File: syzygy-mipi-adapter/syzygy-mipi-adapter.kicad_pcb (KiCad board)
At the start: 4 copper layers, 45 x 70 mm, 98 parts, among them J1 Conn_02x06_Odd_Even, J2 SYZYGY_STD, J3 USB_C_Receptacle_USB2.0_16P, J4 SM03B-SRSS-TB, J6 501951-2230, J7 501951-2230, J8 501951-2230, Q1 DMG1024UV-7, Q2 DMG1024UV-7, U1 RP2350_80QFN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

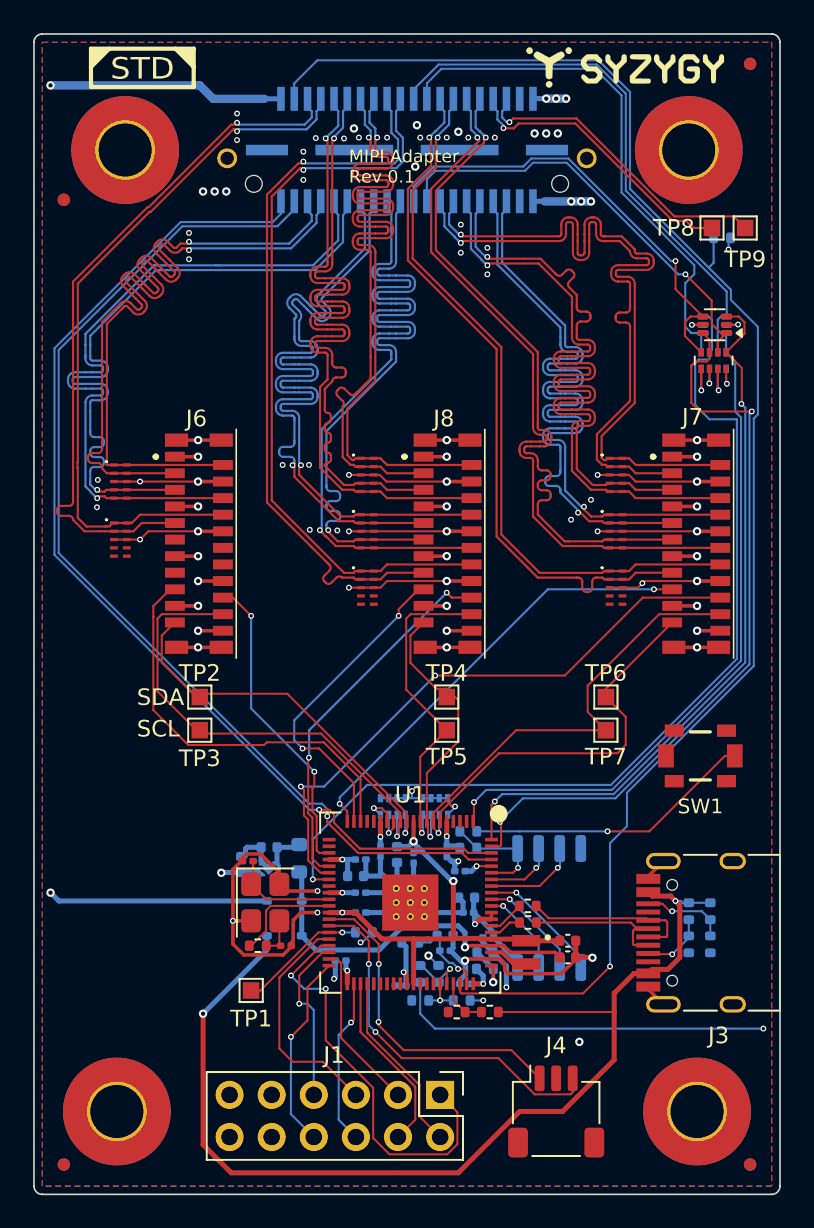
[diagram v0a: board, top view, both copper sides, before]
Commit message: Update stack-up. Adjust DP trace width and spacing to 100 ohm impedance.
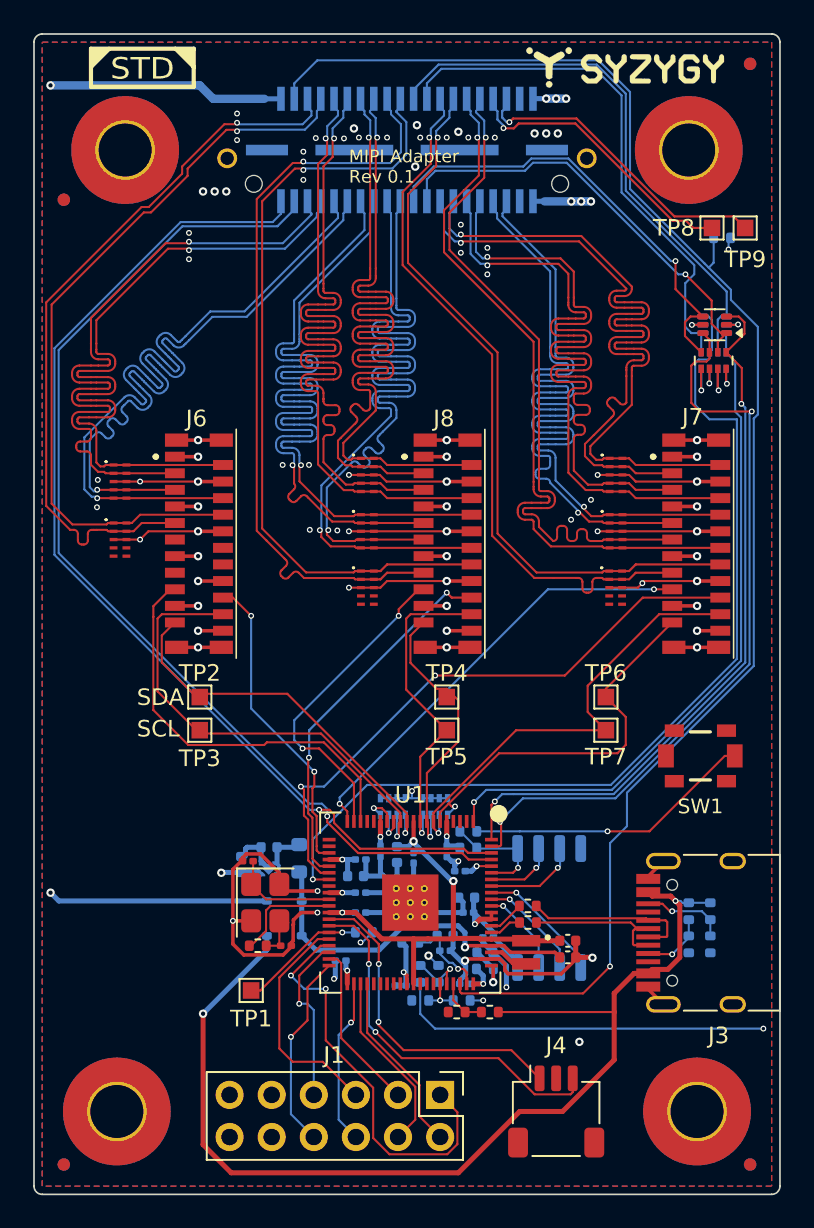
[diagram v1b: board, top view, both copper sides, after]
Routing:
- net /D0N: track 43.2 -> 45.2 mm
- net /D0P: track 42.1 -> 44.1 mm
- net /D3N: track 44.0 -> 46.0 mm
- net /D7P: track 44.3 -> 46.3 mm
- net /D7N: track 45.3 -> 47.3 mm
- net /D4N: track 45.1 -> 47.1 mm
- net /D4P: track 44.1 -> 46.1 mm
- net /D1N: track 43.4 -> 45.3 mm
- net /D1P: track 42.3 -> 44.3 mm
- net /D2P: track 43.2 -> 45.2 mm
- net /D2N: track 42.1 -> 44.1 mm
- net /D6N: track 44.1 -> 46.0 mm
- net /D6P: track 45.2 -> 47.1 mm
- net /D3P: track 45.2 -> 47.1 mm
- net /D5P: track 44.1 -> 46.1 mm
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
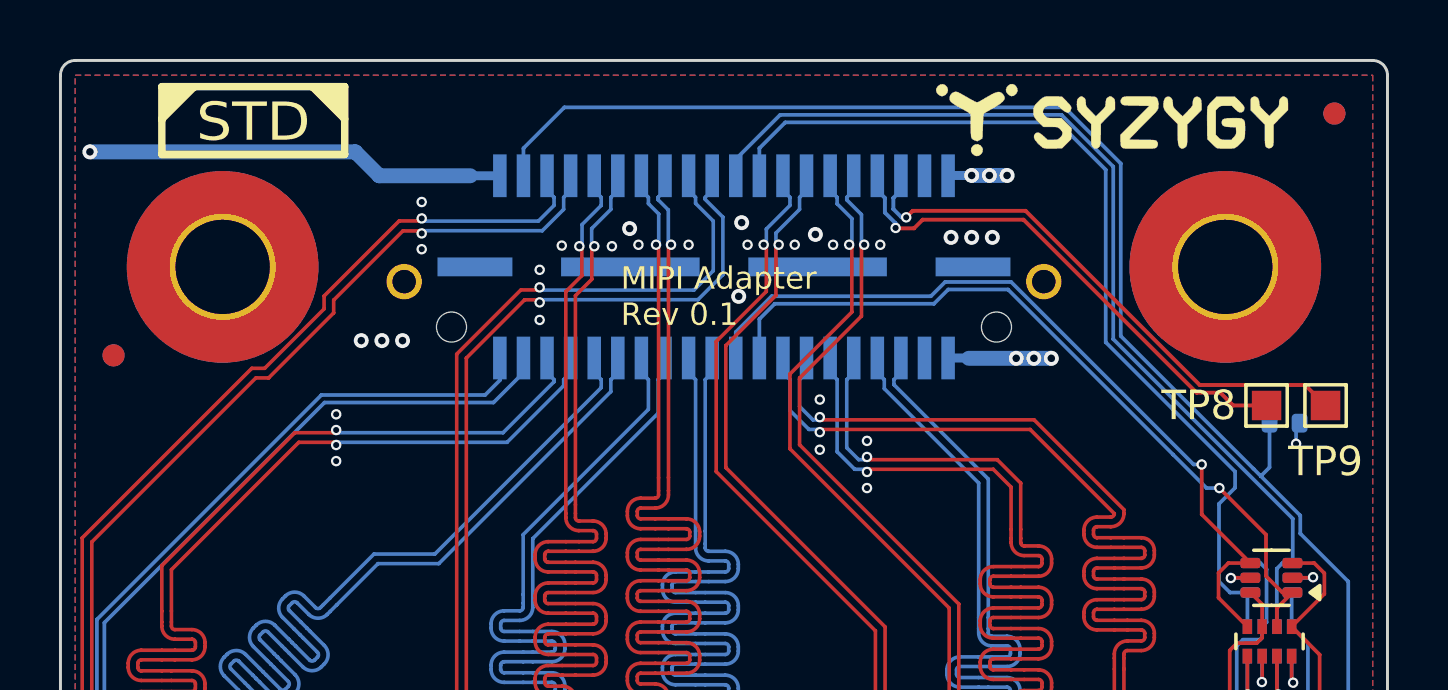
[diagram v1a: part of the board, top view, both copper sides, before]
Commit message: Made tinyvision logo bigger
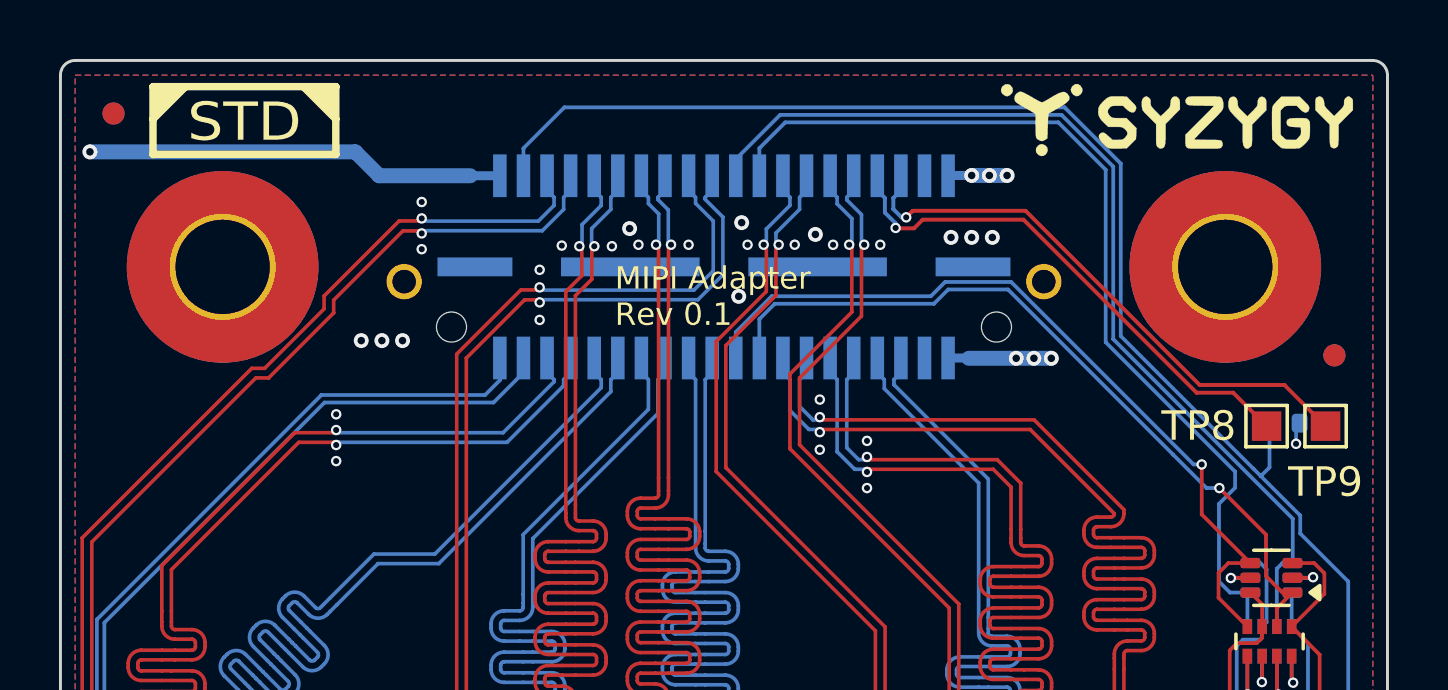
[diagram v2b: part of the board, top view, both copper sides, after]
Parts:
- C38: value 2.2u -> 10u
- LOGO4: footprint CUSTOM:tinyAI_logo -> CUSTOM:tinyAI_4_5mm
- moved FID1 8.20 mm to (101.8, 61.8)
- moved FID2 8.20 mm to (143.2, 70.0)
- moved FID5 8.20 mm to (101.8, 61.8)
- moved FID6 8.20 mm to (143.2, 70.0)
- moved LOGO2 2.20 mm to (137.8, 62.0)
- moved TP8 0.70 mm to (140.9, 72.4)
- moved TP9 0.70 mm to (142.9, 72.4)
- moved LOGO1 0.30 mm to (109.3, 63.2)

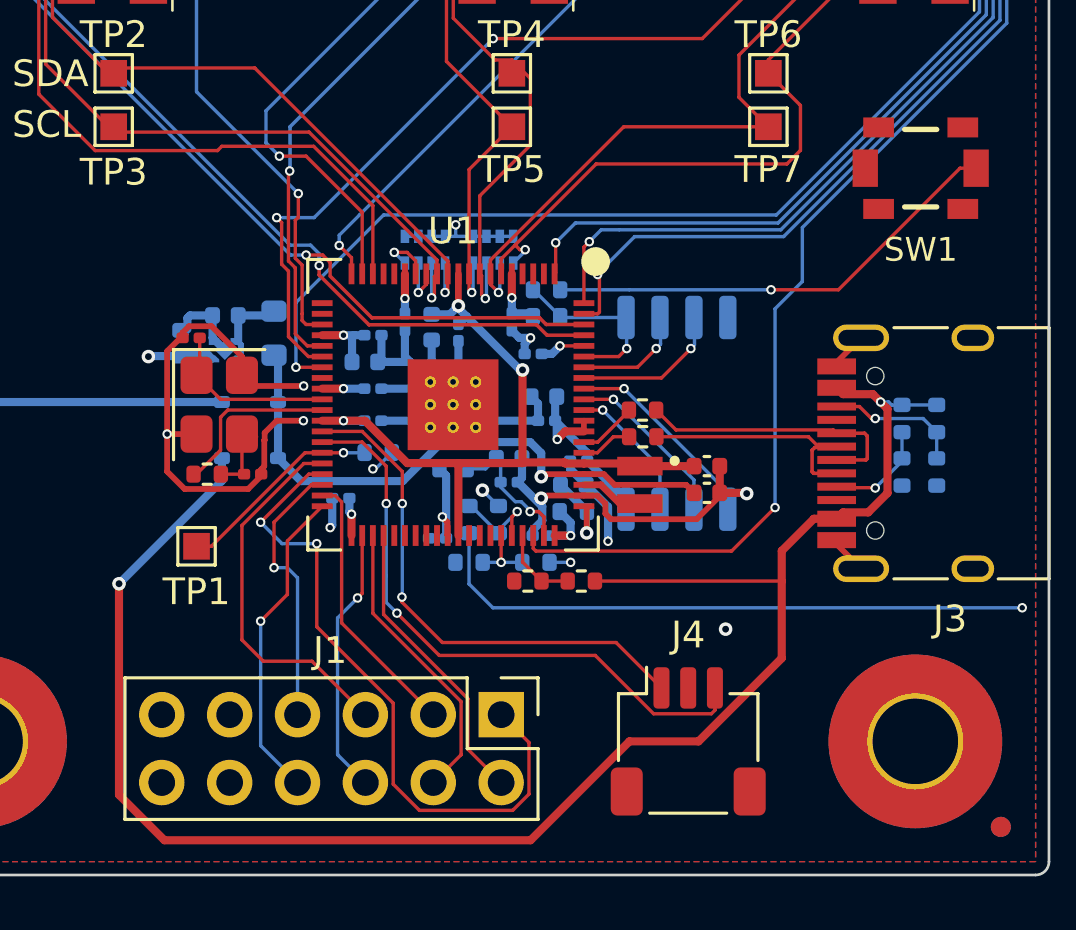
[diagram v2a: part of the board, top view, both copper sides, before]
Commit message: Add a few more vias
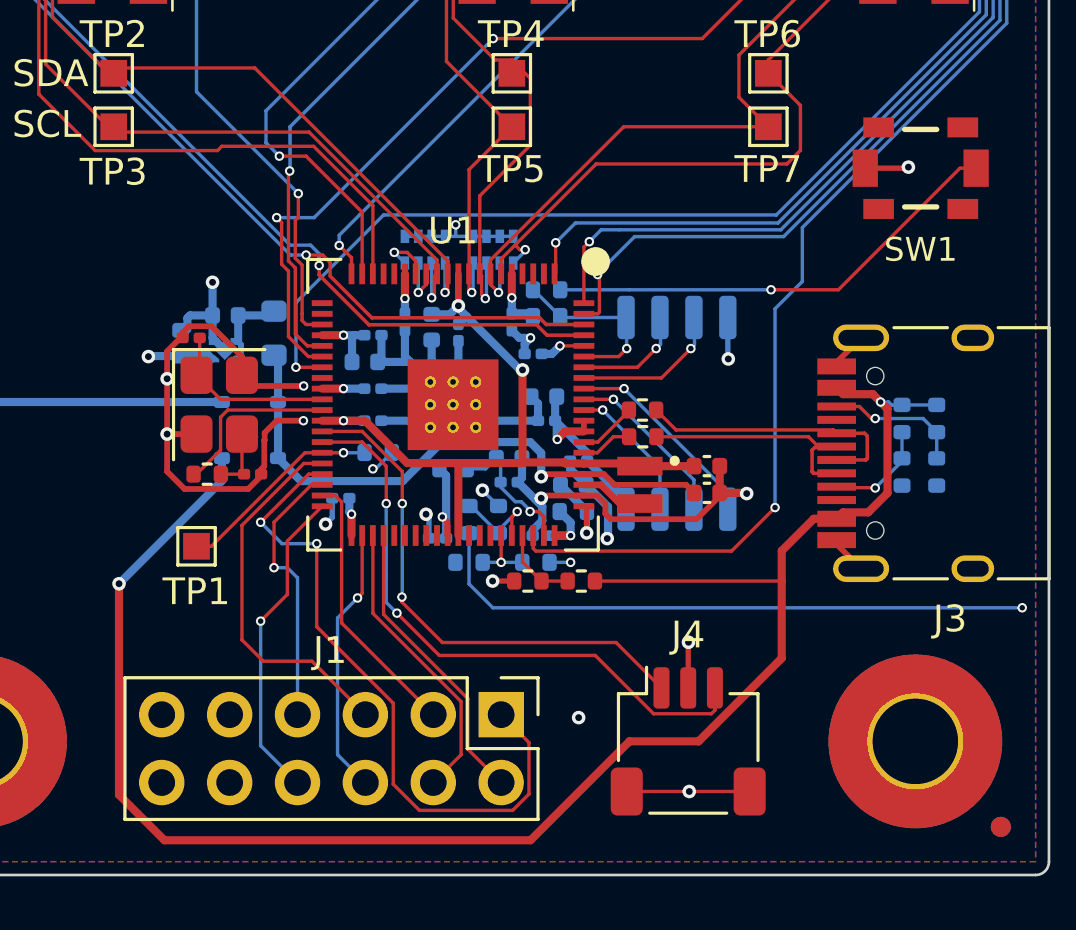
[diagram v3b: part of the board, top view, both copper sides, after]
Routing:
- net GND: track 156.0 -> 168.4 mm, vias 81 -> 89
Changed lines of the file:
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@@
 			(keep_text_aligned yes)
 		)
-		(gr_text "5.0 mm"
+		(gr_text "196.9 mils"
 			(at 95.1 126.3 90)
 			(layer "Dwgs.User")
@@
 			(keep_text_aligned yes)
 		)
-		(gr_text "6.0 mm"
+		(gr_text "236.2 mils"
 			(at 90.6 126.5 90)
 			(layer "Dwgs.User")
@@
 			(keep_text_aligned yes)
 		)
-		(gr_text "24.5 mm"
+		(gr_text "964.6 mils"
 			(at 112.25 137.95 0)
 			(layer "Dwgs.User")
@@
 			(keep_text_aligned yes)
 		)
-		(gr_text "13.260 mm"
+		(gr_text "522.060 mils"
 			(at 106.63016 50.35 0)
 			(layer "Dwgs.User")
@@
 			(keep_text_aligned yes)
 		)
-		(gr_text "9.04 mm"
+		(gr_text "355.91 mils"
 			(at 90.6 64.5 90)
 			(layer "Dwgs.User")
@@
 			(keep_text_aligned yes)
 		)
-		(gr_text "5.0 mm"
+		(gr_text "196.9 mils"
 			(at 103.4 134.3 0)
 			(layer "Dwgs.User")
@@
 			(keep_text_aligned yes)
 		)
-		(gr_text "12.0000 mm"
+		(gr_text "472.4406 mils"
 			(at 148.55 66.000005 90)
 			(layer "Dwgs.User")
@@
 	)
 	(segment
+		(start 138.125 103.55)
+		(end 139.7 103.55)
+		(width 0.2)
+		(layer "F.Cu")
+		(net 2)
+	)
+	(segment
 		(start 115.63595 114.70405)
 		(end 115.52 114.82)
@@
 	(segment
 		(start 112 110.4)
-		(end 112 113.5)
+		(end 112 111.43)
 		(width 0.2159)
 		(layer "F.Cu")
@@
 	)
 	(segment
+		(start 131.5 121.3)
+		(end 131.51 121.29)
+		(width 0.2)
+		(layer "F.Cu")
+		(net 2)
+	)
+	(segment
 		(start 104.824 90.5)
 		(end 105.6 90.5)
@@
 	)
 	(segment
+		(start 131.54 126.875)
+		(end 133.8 126.875)
+		(width 0.127)
+		(layer "F.Cu")
+		(net 2)
+	)
+	(segment
 		(start 115.031926 115.55595)
 		(end 112.65595 115.55595)
@@
 	)
 	(segment
+		(start 131.5 123)
+		(end 131.5 121.3)
+		(width 0.2)
+		(layer "F.Cu")
+		(net 2)
+	)
+	(segment
 		(start 135.5 86.6)
 		(end 135.9 86.6)
@@
 	)
 	(segment
+		(start 112 111.43)
+		(end 112 113.5)
+		(width 0.2159)
+		(layer "F.Cu")
+		(net 2)
+	)
+	(segment
 		(start 137.055 110.813475)
 		(end 137.97 109.898475)
@@
 	)
 	(segment
+		(start 139.7 103.55)
+		(end 139.74 103.51)
+		(width 0.2)
+		(layer "F.Cu")
+		(net 2)
+	)
+	(segment
 		(start 141.3 97)
 		(end 140 97)
@@
 	)
 	(segment
+		(start 129.2 126.875)
+		(end 131.54 126.875)
+		(width 0.127)
+		(layer "F.Cu")
+		(net 2)
+	)
+	(segment
 		(start 132.68 115.82)
 		(end 132.68 115.7)
@@
 	)
 	(segment
+		(start 124.99 119)
+		(end 124.18 119)
+		(width 0.2)
+		(layer "F.Cu")
+		(net 2)
+	)
+	(segment
 		(start 119.724 86.6)
 		(end 120.5 86.6)
@@
 	)
 	(via
-		(at 128.5 117.5097)
-		(size 0.3556)
-		(drill 0.2032)
+		(at 128.47 117.41)
+		(size 0.508)
+		(drill 0.254)
 		(layers "F.Cu" "B.Cu")
 		(net 2)
@@
 	)
 	(via
+		(at 133 110.69)
+		(size 0.508)
+		(drill 0.254)
+		(layers "F.Cu" "B.Cu")
+		(net 2)
+	)
+	(via
 		(at 119 90)
 		(size 0.3556)
@@
 	)
 	(via
+		(at 127.4 124.11)
+		(size 0.508)
+		(drill 0.254)
+		(layers "F.Cu" "B.Cu")
+		(free yes)
+		(net 2)
+	)
+	(via
 		(at 125.75 71.5)
 		(size 0.3556)
@@
 	)
 	(via
+		(at 124.18 119)
+		(size 0.508)
+		(drill 0.254)
+		(layers "F.Cu" "B.Cu")
+		(net 2)
+	)
+	(via
+		(at 121.69 116.5)
+		(size 0.508)
+		(drill 0.254)
+		(layers "F.Cu" "B.Cu")
+		(net 2)
+	)
+	(via
 		(at 127.8 66.25)
 		(size 0.3556)
@@
 	)
 	(via
+		(at 131.54 126.875)
+		(size 0.508)
+		(drill 0.254)
+		(layers "F.Cu" "B.Cu")
+		(net 2)
+	)
+	(via
 		(at 109.9 91.5)
 		(size 0.508)
@@
 	)
 	(via
-		(at 132.9 120.8)
-		(size 0.508)
-		(drill 0.254)
-		(layers "F.Cu" "B.Cu")
-		(net 2)
-	)
-	(via
 		(at 133.689396 115.725911)
 		(size 0.508)
@@
 	)
 	(via
+		(at 112 111.43)
+		(size 0.508)
+		(drill 0.254)
+		(layers "F.Cu" "B.Cu")
+		(net 2)
+	)
+	(via
 		(at 109.9 88.5)
 		(size 0.508)
@@
 	)
 	(via
+		(at 131.51 121.29)
+		(size 0.508)
+		(drill 0.254)
+		(layers "F.Cu" "B.Cu")
+		(net 2)
+	)
+	(via
 		(at 106.4 87)
 		(size 0.3556)
@@
 	)
 	(via
-		(at 118.1 117)
-		(size 0.3556)
-		(drill 0.2032)
+		(at 117.93 116.87)
+		(size 0.508)
+		(drill 0.254)
 		(layers "F.Cu" "B.Cu")
 		(net 2)
@@
 	(via
 		(at 112 113.5)
-		(size 0.3556)
-		(drill 0.2032)
+		(size 0.508)
+		(drill 0.254)
 		(layers "F.Cu" "B.Cu")
 		(net 2)
@@
 	)
 	(via
+		(at 113.7 107.82)
+		(size 0.508)
+		(drill 0.254)
+		(layers "F.Cu" "B.Cu")
+		(net 2)
+	)
+	(via
 		(at 109.9 90)
 		(size 0.508)
@@
 		(layers "F.Cu" "B.Cu")
 		(free yes)
+		(net 2)
+	)
+	(via
+		(at 139.74 103.51)
+		(size 0.508)
+		(drill 0.254)
+		(layers "F.Cu" "B.Cu")
 		(net 2)
 	)
@@
 	)
 	(segment
+		(start 121.8 116.61)
+		(end 121.69 116.5)
+		(width 0.2)
+		(layer "B.Cu")
+		(net 2)
+	)
+	(segment
 		(start 121.1 110.8)
 		(end 121.85 111.55)
@@
 	)
 	(segment
+		(start 128.5 116.22)
+		(end 128.5 117.38)
+		(width 0.3048)
+		(layer "B.Cu")
+		(net 2)
+	)
+	(segment
 		(start 125.38 110.5)
 		(end 125.38 110.12)
@@
 	)
 	(segment
+		(start 118.18 115.9)
+		(end 118.18 116.62)
+		(width 0.2)
+		(layer "B.Cu")
+		(net 2)
+	)
+	(segment
 		(start 124.39 116.19)
 		(end 124.4 116.19)
@@
 	)
 	(segment
+		(start 113.7 109.06)
+		(end 113.7 107.82)
+		(width 0.3048)
+		(layer "B.Cu")
+		(net 2)
+	)
+	(segment
 		(start 121.25 111.8)
 		(end 121.85 112.4)
@@
 	)
 	(segment
+		(start 132.983396 109.1375)
+		(end 132.983396 110.673396)
+		(width 0.2)
+		(layer "B.Cu")
+		(net 2)
+	)
+	(segment
 		(start 120.02 111.8)
 		(end 121.25 111.8)
@@
 	)
 	(segment
-		(start 128.5 116.22)
-		(end 128.5 117.5097)
-		(width 0.3048)
-		(layer "B.Cu")
-		(net 2)
-	)
-	(segment
-		(start 118.18 115.9)
-		(end 118.18 116.92)
-		(width 0.3048)
+		(start 132.983396 110.673396)
+		(end 133 110.69)
+		(width 0.2)
+		(layer "B.Cu")
+		(net 2)
+	)
+	(segment
+		(start 118.18 116.62)
+		(end 117.93 116.87)
+		(width 0.2)
 		(layer "B.Cu")
 		(net 2)
@@
 	)
 	(segment
+		(start 121.8 117.4)
+		(end 121.8 116.61)
+		(width 0.2)
+		(layer "B.Cu")
+		(net 2)
+	)
+	(segment
+		(start 128.5 117.38)
+		(end 128.47 117.41)
+		(width 0.3048)
+		(layer "B.Cu")
+		(net 2)
+	)
+	(segment
 		(start 121.9 109.98)
 		(end 121.9 110.75)
 		(width 0.3048)
 		(layer "B.Cu")
-		(net 2)
-	)
-	(segment
-		(start 118.18 116.92)
-		(end 118.1 117)
-		(width 0.3048)
-		(layer "B.Cu")
